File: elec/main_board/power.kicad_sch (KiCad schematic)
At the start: 45 parts, among them J10 Conn_01x02, J11 B2B-XH-A(LF)(SN), J15 GT-USB-7055E, J16 B4B-ZR(LF)(SN), J9 MJ-179PH, Q5 DMT6008LFG, Q6 DMT6008LFG, Q7 DTC114E, Q8 DTC114E, SW1 B3U-1000P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

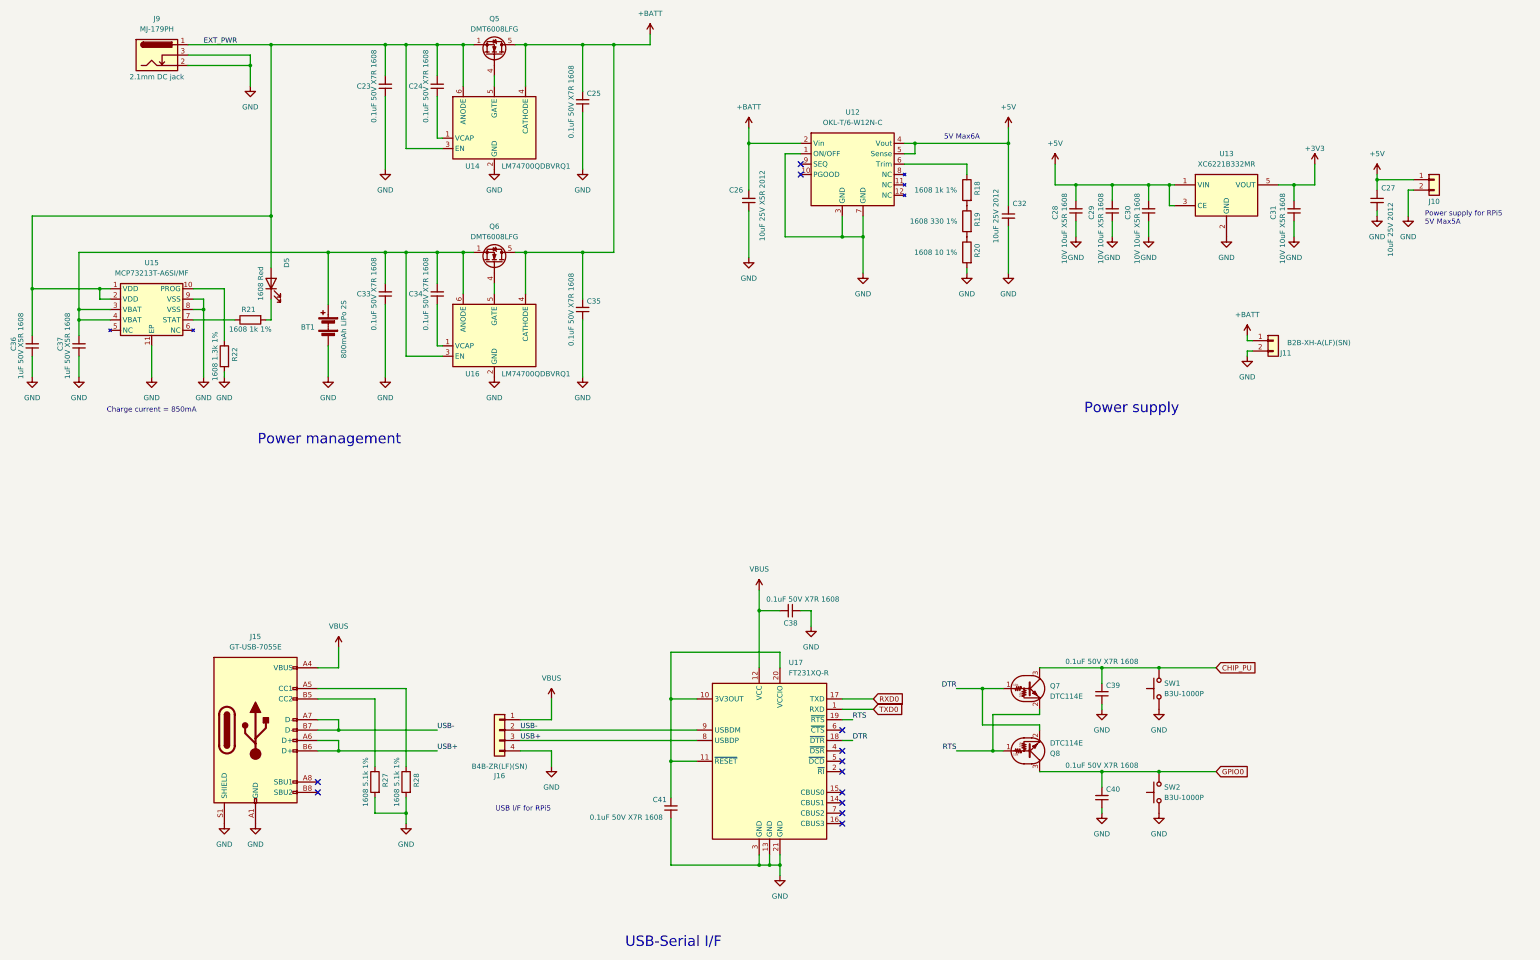
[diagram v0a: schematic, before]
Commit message: 再設計　部品配置完了
Signed-off-by: Kazuki Iida <elkel53930@gmail.com>
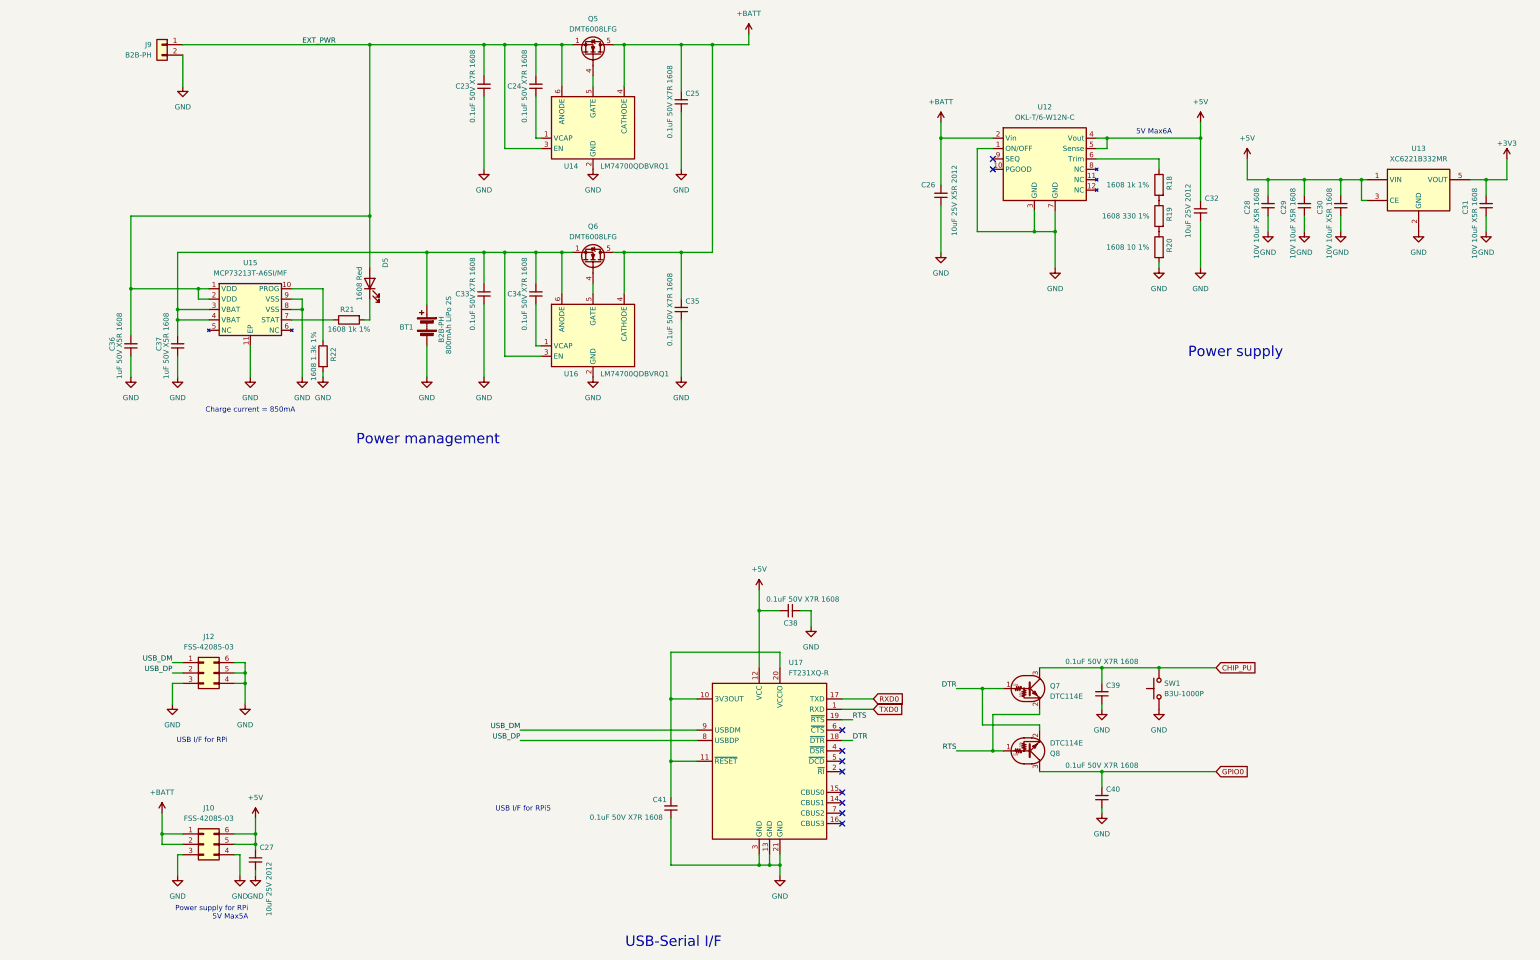
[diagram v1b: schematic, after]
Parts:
- removed J10: Conn_01x02, Connector_JST:JST_PH_B2B-PH-K_1x02_P2.00mm_Vertical, symbol Connector_Generic:Conn_01x02
- removed J11: B2B-XH-A(LF)(SN), Connector_JST:JST_PH_B2B-PH-K_1x02_P2.00mm_Vertical, symbol Connector_Generic:Conn_01x02
- removed J15: GT-USB-7055E, Library:USB-C-SMD_GT-USB-7055E, symbol Connector:USB_C_Receptacle_USB2.0_16P
- removed J16: B4B-ZR(LF)(SN), Connector_JST:JST_ZH_B4B-ZR_1x04_P1.50mm_Vertical, symbol Connector_Generic:Conn_01x04
- removed J9: MJ-179PH, Library:PJ-002A, symbol Connector:Barrel_Jack_Switch
- removed R27, R28: 0603WAF5101T5E, Resistor_SMD:R_0603_1608Metric, symbol Device:R
- removed SW2: B3U-1000P, Button_Switch_SMD:SW_SPST_B3U-1000P, symbol Switch:SW_Push
- added J10, J12: FSS-42085-03, Connector_PinHeader_2.54mm:PinHeader_2x03_P2.54mm_Vertical, symbol Connector_Generic:Conn_02x03_Counter_Clockwise
- added J9: B2B-PH, Connector_JST:JST_PH_B2B-PH-K_1x02_P2.00mm_Vertical, symbol Connector_Generic:Conn_01x02
- BT1: value 800mAh LiPo 2S -> B2B-PH
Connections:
- net VBUS is gone; now on net +5V: C38.2, U17.12 (VCC)
- net +5V: now also J10.5 (Pin_5), J10.6 (Pin_6)
- net +BATT: now also J10.1 (Pin_1), J10.2 (Pin_2)
- net EXT_PWR: now also J9.1 (Pin_1)
- net GND: now also J10.3 (Pin_3), J10.4 (Pin_4), J12.3 (Pin_3), J12.4 (Pin_4), J12.5 (Pin_5), J12.6 (Pin_6), J9.2 (Pin_2)
- net USB+ renamed USB_DP
- net USB_DP: now also J12.2 (Pin_2)
- net USB- renamed USB_DM
- net USB_DM: now also J12.1 (Pin_1)
- no-connect marks 12 -> 10
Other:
- note added: "Power supply for RPi 5V Max5A"
- note added: "USB I/F for RPi"
- note removed: "Power supply for RPi5 5V Max5A"
- moved on the sheet: BT1, C23, C24, C25, C26, C27, C28, C29, C30, C31, C32, C33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

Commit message: 配線作業中
Signed-off-by: Kazuki Iida <elkel53930@gmail.com>
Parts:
- C39: value CC0603KRX7R9BB104 -> CL10A105KB8NNNC
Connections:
- net +5V: no longer C38.2, U17.12 (VCC)
- net GND: no longer J12.3 (Pin_3)
- new net VBUS: C38.2, J12.3 (Pin_3), U17.12 (VCC)
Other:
- note added: "DC power source"
- note added: "Reset switch"
- note removed: "USB I/F for RPi5"
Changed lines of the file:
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@@
 		)
 	)
+	(text "DC power source"
+		(exclude_from_sim no)
+		(at 35.052 41.91 0)
+		(effects
+			(font
+				(size 1.27 1.27)
+			)
+			(justify left bottom)
+		)
+	)
 	(text "Power supply for RPi\n5V Max5A"
 		(exclude_from_sim no)
@@
 		)
 	)
-	(text "USB I/F for RPi5\n"
+	(text "USB I/F for RPi"
+		(exclude_from_sim no)
+		(at 140.97 217.17 0)
+		(effects
+			(font
+				(size 1.27 1.27)
+			)
+			(justify left bottom)
+		)
+	)
+	(text "Reset switch"
 		(exclude_from_sim no)
-		(at 146.304 228.346 0)
+		(at 313.69 205.232 0)
 		(effects
 			(font
@@
 	(wire
 		(pts
-			(xy 67.31 196.85) (xy 69.85 196.85)
-		)
-		(stroke
-			(width 0)
-			(type default)
-		)
-	)
-	(wire
-		(pts
 			(xy 57.15 100.33) (xy 57.15 111.76)
 		)
@@
 	(wire
 		(pts
-			(xy 67.31 191.77) (xy 69.85 191.77)
+			(xy 58.42 191.77) (xy 69.85 191.77)
 		)
 		(stroke
@@
 	(wire
 		(pts
+			(xy 63.5 196.85) (xy 69.85 196.85)
+		)
+		(stroke
+			(width 0)
+			(type default)
+		)
+	)
+	(wire
+		(pts
 			(xy 335.28 82.55) (xy 335.28 86.36)
 		)
@@
 	(wire
 		(pts
+			(xy 63.5 185.42) (xy 63.5 196.85)
+		)
+		(stroke
+			(width 0)
+			(type default)
+		)
+	)
+	(wire
+		(pts
 			(xy 191.77 107.95) (xy 191.77 121.92)
 		)
@@
 	(wire
 		(pts
-			(xy 67.31 194.31) (xy 69.85 194.31)
+			(xy 58.42 194.31) (xy 69.85 194.31)
 		)
 		(stroke
@@
 	(wire
 		(pts
-			(xy 67.31 196.85) (xy 67.31 201.93)
-		)
-		(stroke
-			(width 0)
-			(type default)
-		)
-	)
-	(wire
-		(pts
 			(xy 318.77 63.5) (xy 318.77 78.74)
 		)
@@
 	)
 	(label "USB_DP"
-		(at 67.31 194.31 180)
+		(at 58.42 194.31 180)
 		(effects
 			(font
@@
 	)
 	(label "USB_DM"
-		(at 67.31 191.77 180)
+		(at 58.42 191.77 180)
 		(effects
 			(font
@@
 			)
 		)
-		(property "Value" "CC0603KRX7R9BB104"
+		(property "Value" "CL10A105KB8NNNC"
 			(at 298.45 207.01 90)
 			(effects
@@
 			)
 		)
-		(property "Description" "0.1uF 50V X7R 1608"
+		(property "Description" "1uF 50V X5R 1608"
 			(at 294.64 191.516 0)
 			(effects
@@
 	)
 	(symbol
+		(lib_id "power:VBUS")
+		(at 210.82 173.99 0)
+		(unit 1)
+		(exclude_from_sim no)
+		(in_bom yes)
+		(on_board yes)
+		(dnp no)
+		(fields_autoplaced yes)
+		(property "Reference" "#PWR044"
+			(at 210.82 177.8 0)
+			(effects
+				(font
+					(size 1.27 1.27)
+				)
+				(hide yes)
+			)
+		)
+		(property "Value" "VBUS"
+			(at 210.82 168.91 0)
+			(effects
+				(font
+					(size 1.27 1.27)
+				)
+			)
+		)
+		(property "Footprint" ""
+			(at 210.82 173.99 0)
+			(effects
+				(font
+					(size 1.27 1.27)
+				)
+				(hide yes)
+			)
+		)
+		(property "Datasheet" ""
+			(at 210.82 173.99 0)
+			(effects
+				(font
+					(size 1.27 1.27)
+				)
+				(hide yes)
+			)
+		)
+		(property "Description" "Power symbol creates a global label with name \"VBUS\""
+			(at 210.82 173.99 0)
+			(effects
+				(font
+					(size 1.27 1.27)
+				)
+				(hide yes)
+			)
+		)
+		(pin "1"
+		)
+		(instances
+			(project ""
+				(path "/d2cf6a41-8170-4aa9-b19e-2c9825cc9c77/829ce076-7c19-4bad-87be-13e3998cb698"
+					(reference "#PWR044")
+					(unit 1)
+				)
+			)
+		)
+	)
+	(symbol
 		(lib_id "power:GND")
 		(at 388.62 86.36 0)
@@
 	)
 	(symbol
-		(lib_id "power:+5V")
-		(at 210.82 173.99 0)
-		(unit 1)
-		(exclude_from_sim no)
-		(in_bom yes)
-		(on_board yes)
-		(dnp no)
-		(fields_autoplaced yes)
-		(property "Reference" "#PWR053"
-			(at 210.82 177.8 0)
-			(effects
-				(font
-					(size 1.27 1.27)
-				)
-				(hide yes)
-			)
-		)
-		(property "Value" "+5V"
-			(at 210.82 168.91 0)
-			(effects
-				(font
-					(size 1.27 1.27)
-				)
-			)
-		)
-		(property "Footprint" ""
-			(at 210.82 173.99 0)
-			(effects
-				(font
-					(size 1.27 1.27)
-				)
-				(hide yes)
-			)
-		)
-		(property "Datasheet" ""
-			(at 210.82 173.99 0)
-			(effects
-				(font
-					(size 1.27 1.27)
-				)
-				(hide yes)
-			)
-		)
-		(property "Description" "Power symbol creates a global label with name \"+5V\""
-			(at 210.82 173.99 0)
-			(effects
-				(font
-					(size 1.27 1.27)
-				)
-				(hide yes)
-			)
-		)
-		(pin "1"
-		)
-		(instances
-			(project "main_board"
-				(path "/d2cf6a41-8170-4aa9-b19e-2c9825cc9c77/829ce076-7c19-4bad-87be-13e3998cb698"
-					(reference "#PWR053")
-					(unit 1)
-				)
-			)
-		)
-	)
-	(symbol
 		(lib_id "power:GND")
 		(at 335.28 86.36 0)
@@
 	)
 	(symbol
-		(lib_id "power:GND")
-		(at 67.31 201.93 0)
-		(unit 1)
-		(exclude_from_sim no)
-		(in_bom yes)
-		(on_board yes)
-		(dnp no)
-		(fields_autoplaced yes)
-		(property "Reference" "#PWR045"
-			(at 67.31 208.28 0)
-			(effects
-				(font
-					(size 1.27 1.27)
-				)
-				(hide yes)
-			)
-		)
-		(property "Value" "GND"
-			(at 67.31 207.01 0)
-			(effects
-				(font
-					(size 1.27 1.27)
-				)
-			)
-		)
-		(property "Footprint" ""
-			(at 67.31 201.93 0)
-			(effects
-				(font
-					(size 1.27 1.27)
-				)
-				(hide yes)
-			)
-		)
-		(property "Datasheet" ""
-			(at 67.31 201.93 0)
-			(effects
-				(font
-					(size 1.27 1.27)
-				)
-				(hide yes)
-			)
-		)
-		(property "Description" ""
-			(at 67.31 201.93 0)
-			(effects
-				(font
-					(size 1.27 1.27)
-				)
-			)
-		)
-		(pin "1"
-		)
-		(instances
-			(project "main_board"
-				(path "/d2cf6a41-8170-4aa9-b19e-2c9825cc9c77/829ce076-7c19-4bad-87be-13e3998cb698"
-					(reference "#PWR045")
-					(unit 1)
-				)
-			)
-		)
-	)
-	(symbol
 		(lib_id "Transistor_FET:DMT6008LFG")
 		(at 170.18 43.18 270)
@@
 					(unit 1)
 				)
+			)
+		)
+	)
+	(symbol
+		(lib_id "power:VBUS")
+		(at 63.5 185.42 0)
+		(unit 1)
+		(exclude_from_sim no)
+		(in_bom yes)
+		(on_board yes)
+		(dnp no)
+		(fields_autoplaced yes)
+		(property "Reference" "#PWR045"
+			(at 63.5 189.23 0)
+			(effects
+				(font
+					(size 1.27 1.27)
+				)
+				(hide yes)
+			)
+		)
+		(property "Value" "VBUS"
+			(at 63.5 180.34 0)
+			(effects
+				(font
+					(size 1.27 1.27)
+				)
+			)
+		)
+		(property "Footprint" ""
+			(at 63.5 185.42 0)
+			(effects
+				(font
+					(size 1.27 1.27)
+				)
+				(hide yes)
+			)
+		)
+		(property "Datasheet" ""
+			(at 63.5 185.42 0)
+			(effects
+				(font
+					(size 1.27 1.27)
+				)
+				(hide yes)
+			)
+		)
+		(property "Description" "Power symbol creates a global label with name \"VBUS\""
+			(at 63.5 185.42 0)
+			(effects
+				(font
+					(size 1.27 1.27)
+				)
+				(hide yes)
+			)
+		)
+		(pin "1"
+		)
+		(instances
+			(project "main_board"
+				(path "/d2cf6a41-8170-4aa9-b19e-2c9825cc9c77/829ce076-7c19-4bad-87be-13e3998cb698"
+					(reference "#PWR045")
+					(unit 1)
+				)
